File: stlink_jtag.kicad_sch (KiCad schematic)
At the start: 15 parts, among them J1301 Conn_01x06_Pin, J1302 Conn_01x04_Pin

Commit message: fixed like a bunch of things, power and new xcvr and lights and other goodies, also started layout
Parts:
- J1801: renamed from J1301; footprint (none) -> Connector_PinHeader_2.54mm:PinHeader_1x06_P2.54mm_Vertical
- J1802: renamed from J1302; footprint (none) -> Connector_PinHeader_2.54mm:PinHeader_1x04_P2.54mm_Vertical
- JP1801: renamed from JP1301; footprint (none) -> Jumper:SolderJumper-2_P1.3mm_Bridged_Pad1.0x1.5mm
- JP1802: renamed from JP1302; footprint (none) -> Jumper:SolderJumper-2_P1.3mm_Bridged_Pad1.0x1.5mm
- JP1803: renamed from JP1303; footprint (none) -> Jumper:SolderJumper-2_P1.3mm_Bridged_Pad1.0x1.5mm
- JP1804: renamed from JP1304; footprint (none) -> Jumper:SolderJumper-2_P1.3mm_Bridged_Pad1.0x1.5mm
- JP1805: renamed from JP1305; footprint (none) -> Jumper:SolderJumper-2_P1.3mm_Open_Pad1.0x1.5mm
- JP1806: renamed from JP1306; footprint (none) -> Jumper:SolderJumper-2_P1.3mm_Open_Pad1.0x1.5mm
- JP1807: renamed from JP1307; footprint (none) -> Jumper:SolderJumper-2_P1.3mm_Open_Pad1.0x1.5mm
- JP1808: renamed from JP1308; footprint (none) -> Jumper:SolderJumper-2_P1.3mm_Open_Pad1.0x1.5mm
- renumbered R1301 to R1801, R1302 to R1802, R1303 to R1803, R1304 to R1804, R1305 to R1805
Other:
- moved on the sheet: J1801, J1802, JP1801, JP1802, JP1803, JP1804, JP1805, JP1806, JP1807, JP1808, R1801, R1802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

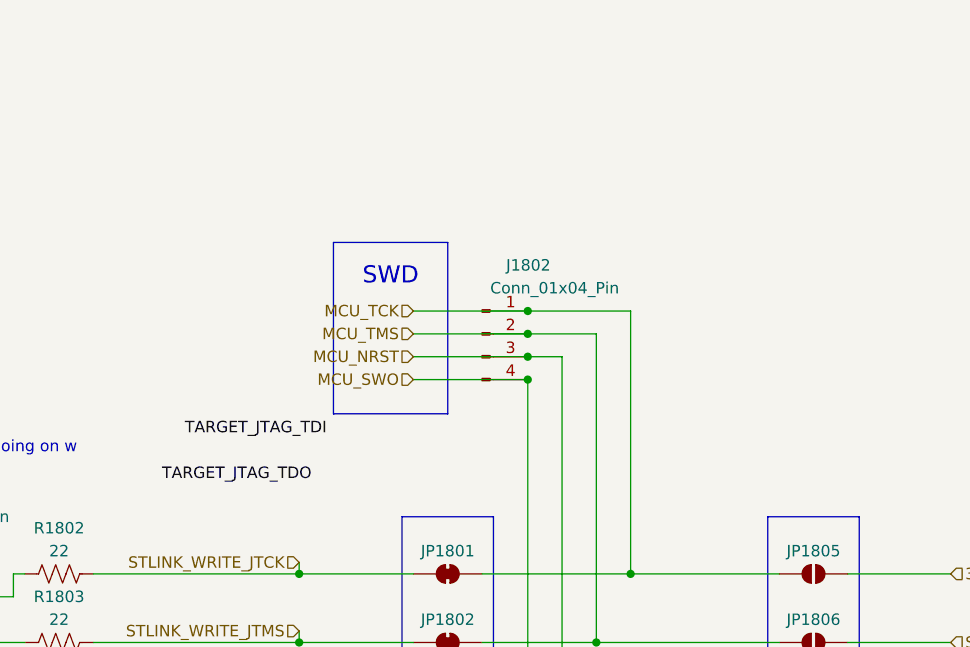
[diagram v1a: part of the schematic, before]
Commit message: laid out most of power, main xcvr, prob some other stuff
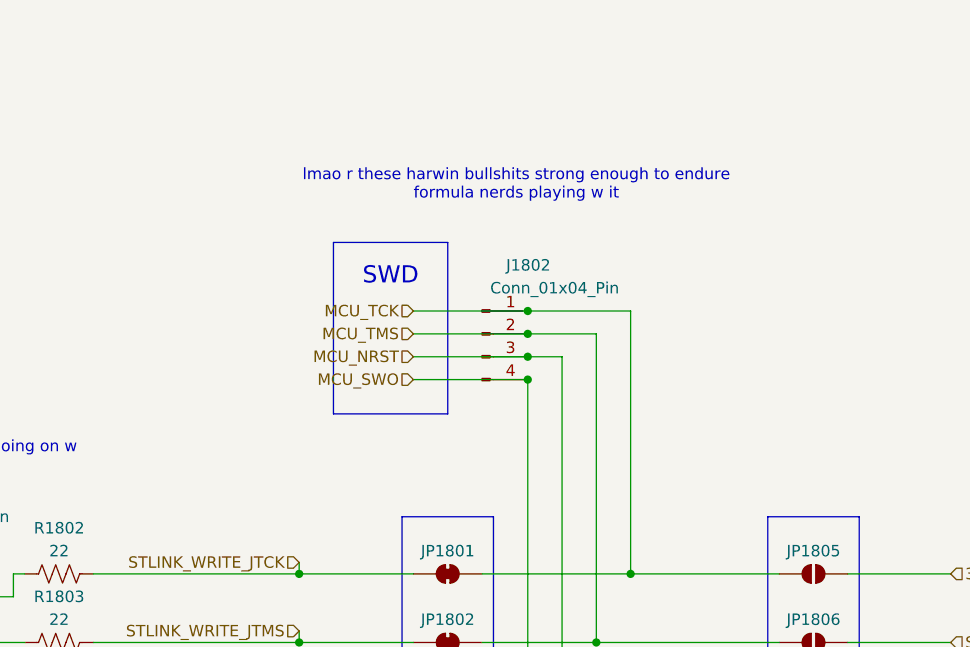
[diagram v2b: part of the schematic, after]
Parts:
- J1801: footprint Connector_PinHeader_2.54mm:PinHeader_1x06_P2.54mm_Vertical -> Connector_PinHeader_2.54mm:PinHeader_1x06_P2.54mm_Vertical_SMD_Pin1Right
- J1802: footprint Connector_PinHeader_2.54mm:PinHeader_1x04_P2.54mm_Vertical -> Connector_PinHeader_2.54mm:PinHeader_1x04_P2.54mm_Vertical_SMD_Pin1Left
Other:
- note added: "lmao r these harwin bullshits strong enough to endure formula nerds playing w it"
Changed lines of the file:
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@@
+		)
+	)
+	(text "lmao r these harwin bullshits strong enough to endure \nformula nerds playing w it"
+		(exclude_from_sim no)
+		(at 151.13 43.18 0)
+		(effects
+			(font
+				(size 1.27 1.27)
+			)
 		)
 	)
@@
 			(width 0)
 			(type default)
-		)
-	)
-	(label "TARGET_JTAG_TDI"
-		(at 114.3 71.12 0)
-		(effects
-			(font
-				(size 1.27 1.27)
-			)
-			(justify left bottom)
-		)
-	)
-	(label "TARGET_JTAG_TDO"
-		(at 111.76 76.2 0)
-		(effects
-			(font
-				(size 1.27 1.27)
-			)
-			(justify left bottom)
 		)
 	)
@@
 			)
 		)
-		(property "Footprint" "Connector_PinHeader_2.54mm:PinHeader_1x04_P2.54mm_Vertical"
+		(property "Footprint" "Connector_PinHeader_2.54mm:PinHeader_1x04_P2.54mm_Vertical_SMD_Pin1Left"
 			(at 147.32 59.69 0)
 			(effects
@@
 		)
 		(property "Description" "Generic connector, single row, 01x04, script generated"
+			(at 147.32 59.69 0)
+			(effects
+				(font
+					(size 1.27 1.27)
+				)
+				(hide yes)
+			)
+		)
+		(property "Manufacturer P/N" ""
+			(at 147.32 59.69 0)
+			(effects
+				(font
+					(size 1.27 1.27)
+				)
+				(hide yes)
+			)
+		)
+		(property "Manufacturer" ""
+			(at 147.32 59.69 0)
+			(effects
+				(font
+					(size 1.27 1.27)
+				)
+				(hide yes)
+			)
+		)
+		(property "Digikey P/N" ""
+			(at 147.32 59.69 0)
+			(effects
+				(font
+					(size 1.27 1.27)
+				)
+				(hide yes)
+			)
+		)
+		(property "Mouser P/N" ""
+			(at 147.32 59.69 0)
+			(effects
+				(font
+					(size 1.27 1.27)
+				)
+				(hide yes)
+			)
+		)
+		(property "LCSC P/N" ""
+			(at 147.32 59.69 0)
+			(effects
+				(font
+					(size 1.27 1.27)
+				)
+				(hide yes)
+			)
+		)
+		(property "JLC Basic Part" ""
+			(at 147.32 59.69 0)
+			(effects
+				(font
+					(size 1.27 1.27)
+				)
+				(hide yes)
+			)
+		)
+		(property "Order From" ""
+			(at 147.32 59.69 0)
+			(effects
+				(font
+					(size 1.27 1.27)
+				)
+				(hide yes)
+			)
+		)
+		(property "Created By" ""
+			(at 147.32 59.69 0)
+			(effects
+				(font
+					(size 1.27 1.27)
+				)
+				(hide yes)
+			)
+		)
+		(property "Pretty Name" ""
 			(at 147.32 59.69 0)
 			(effects
@@
 			)
 		)
-		(property "Footprint" "Connector_PinHeader_2.54mm:PinHeader_1x06_P2.54mm_Vertical"
+		(property "Footprint" "Connector_PinHeader_2.54mm:PinHeader_1x06_P2.54mm_Vertical_SMD_Pin1Right"
 			(at 87.63 91.44 0)
 			(effects
@@
 			(at 87.63 91.44 0)
 			(effects
+				(font
+					(size 1.27 1.27)
+				)
+				(hide yes)
+			)
+		)
+		(property "Manufacturer P/N" ""
+			(at 87.63 91.44 0)
+			(effects
+				(font
+					(size 1.27 1.27)
+				)
+				(hide yes)
+			)
+		)
+		(property "Manufacturer" ""
+			(at 87.63 91.44 0)
+			(effects
+				(font
+					(size 1.27 1.27)
+				)
+				(hide yes)
+			)
+		)
+		(property "Digikey P/N" ""
+			(at 87.63 91.44 0)
+			(effects
+				(font
+					(size 1.27 1.27)
+				)
+				(hide yes)
+			)
+		)
+		(property "Mouser P/N" ""
+			(at 87.63 91.44 0)
+			(effects
+				(font
+					(size 1.27 1.27)
+				)
+				(hide yes)
+			)
+		)
+		(property "LCSC P/N" ""
+			(at 87.63 91.44 0)
+			(effects
+				(font
+					(size 1.27 1.27)
+				)
+				(hide yes)
+			)
+		)
+		(property "JLC Basic Part" ""
+			(at 87.63 91.44 0)
+			(effects
+				(font
+					(size 1.27 1.27)
+				)
+				(hide yes)
+			)
+		)
+		(property "Order From" ""
+			(at 87.63 91.44 0)
+			(effects
+				(font
+					(size 1.27 1.27)
+				)
+				(hide yes)
+			)
+		)
+		(property "Created By" ""
+			(at 87.63 91.44 0)
+			(effects
+				(font
+					(size 1.27 1.27)
+				)
+				(hide yes)
+			)
+		)
+		(property "Pretty Name" ""
+			(at 87.63 91.44 0)
+			(effects

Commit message: fucking shit bro i like expanded the board by 1mm and it still has no room fuck this bitchass crystal
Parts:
- removed J1801: Conn_01x06_Pin, Connector_PinHeader_2.54mm:PinHeader_1x06_P2.54mm_Vertical_SMD_Pin1Right, symbol Connector:Conn_01x06_Pin
- removed J1802: Conn_01x04_Pin, Connector_PinHeader_2.54mm:PinHeader_1x04_P2.54mm_Vertical_SMD_Pin1Left, symbol Connector:Conn_01x04_Pin
- added J1801: Conn_02x05_Odd_Even, Connector_PinHeader_2.54mm:PinHeader_2x05_P2.54mm_Vertical_SMD, symbol Connector_Generic:Conn_02x05_Odd_Even
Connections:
- net GND: now also J1801.2 (Pin_2)
- net MCU_NRST: now also J1801.7 (Pin_7)
- net MCU_SWO: now also J1801.9 (Pin_9)
- net MCU_TCK: now also J1801.3 (Pin_3)
- net MCU_TMS: now also J1801.5 (Pin_5)
- net at R1802.1: now also J1801.4 (Pin_4)
- net +5V: now reaches R1801.2
- net +5V: now also J1801.1 (Pin_1)
- net at R1803.1: now also J1801.6 (Pin_6)
- net at R1804.1: now also J1801.8 (Pin_8)
- net at R1805.1: now also J1801.10 (Pin_10)

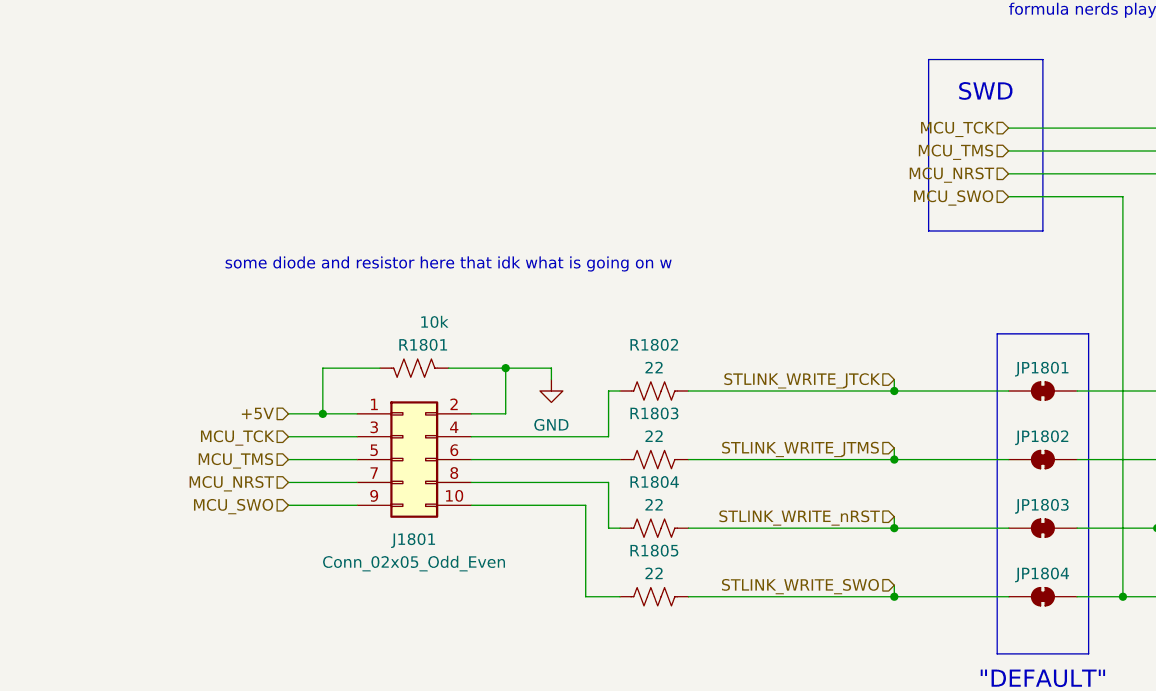
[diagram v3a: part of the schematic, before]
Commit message: small schematic changes, need to reroute
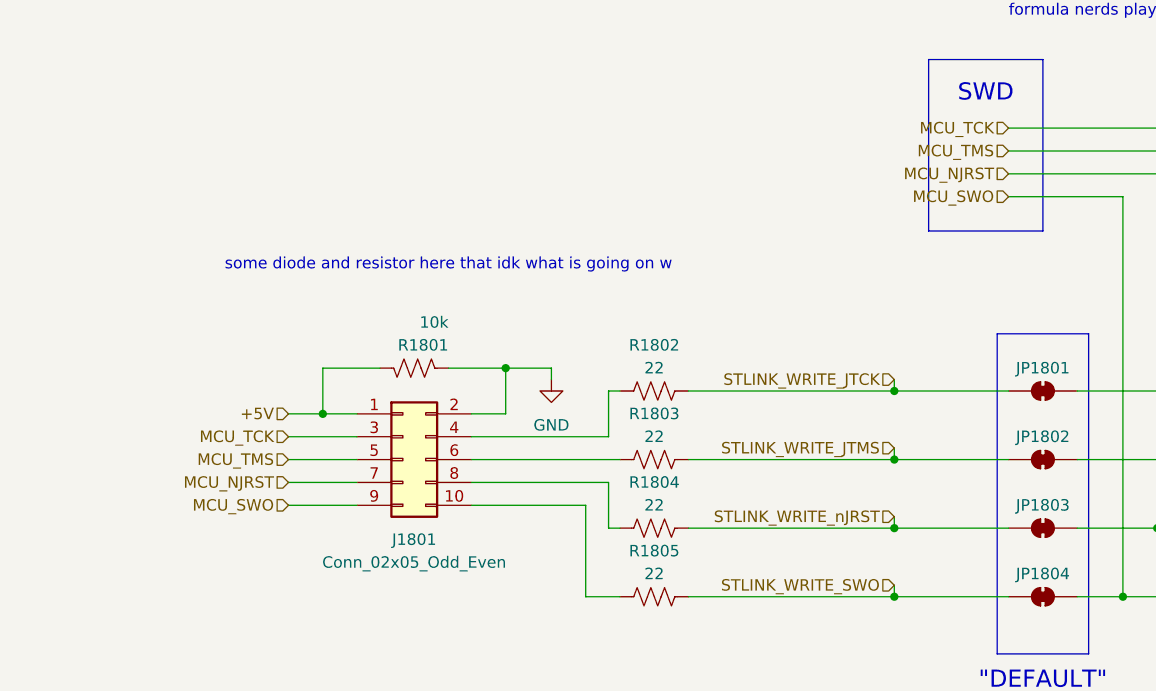
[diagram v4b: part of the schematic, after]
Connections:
- net MCU_NRST renamed MCU_NJRST
- net STLINK_WRITE_nRST renamed STLINK_WRITE_nJRST
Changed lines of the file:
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@@
 		)
 	)
-	(hierarchical_label "MCU_NRST"
+	(hierarchical_label "MCU_NJRST"
 		(shape input)
 		(at 59.69 96.52 180)
@@
 		)
 	)
-	(hierarchical_label "MCU_NRST"
+	(hierarchical_label "MCU_NJRST"
 		(shape input)
 		(at 139.7 62.23 180)
@@
 		)
 	)
-	(hierarchical_label "STLINK_WRITE_nRST"
+	(hierarchical_label "STLINK_WRITE_nJRST"
 		(shape input)
 		(at 127 100.33 180)
